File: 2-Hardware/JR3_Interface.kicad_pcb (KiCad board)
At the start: 2 copper layers, 25.4 x 74.2 mm, 11 parts, among them J1 DB9, J2 CONN_3, J3 CONN_3, P1 HE10-34

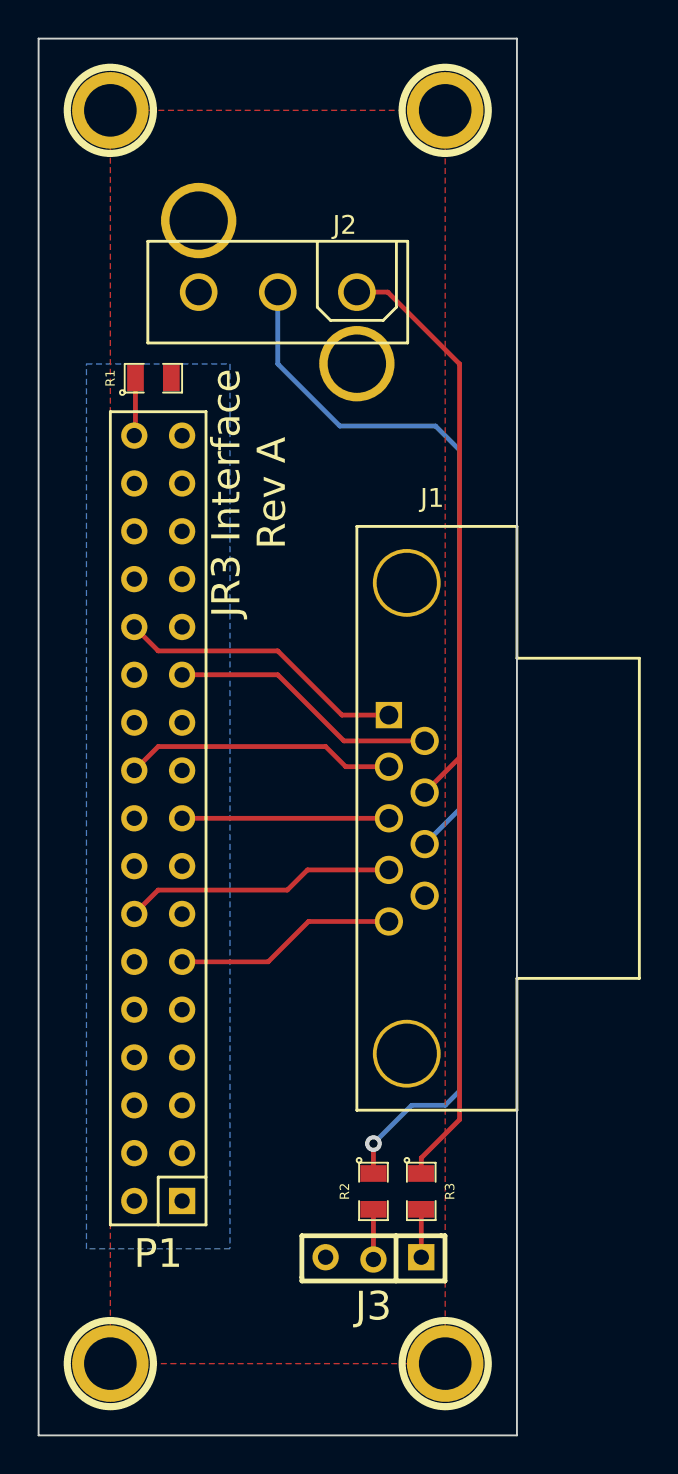
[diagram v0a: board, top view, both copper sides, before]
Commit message: Fixes #5 and resolves #3. Also fixes the power connector footprint on this board.
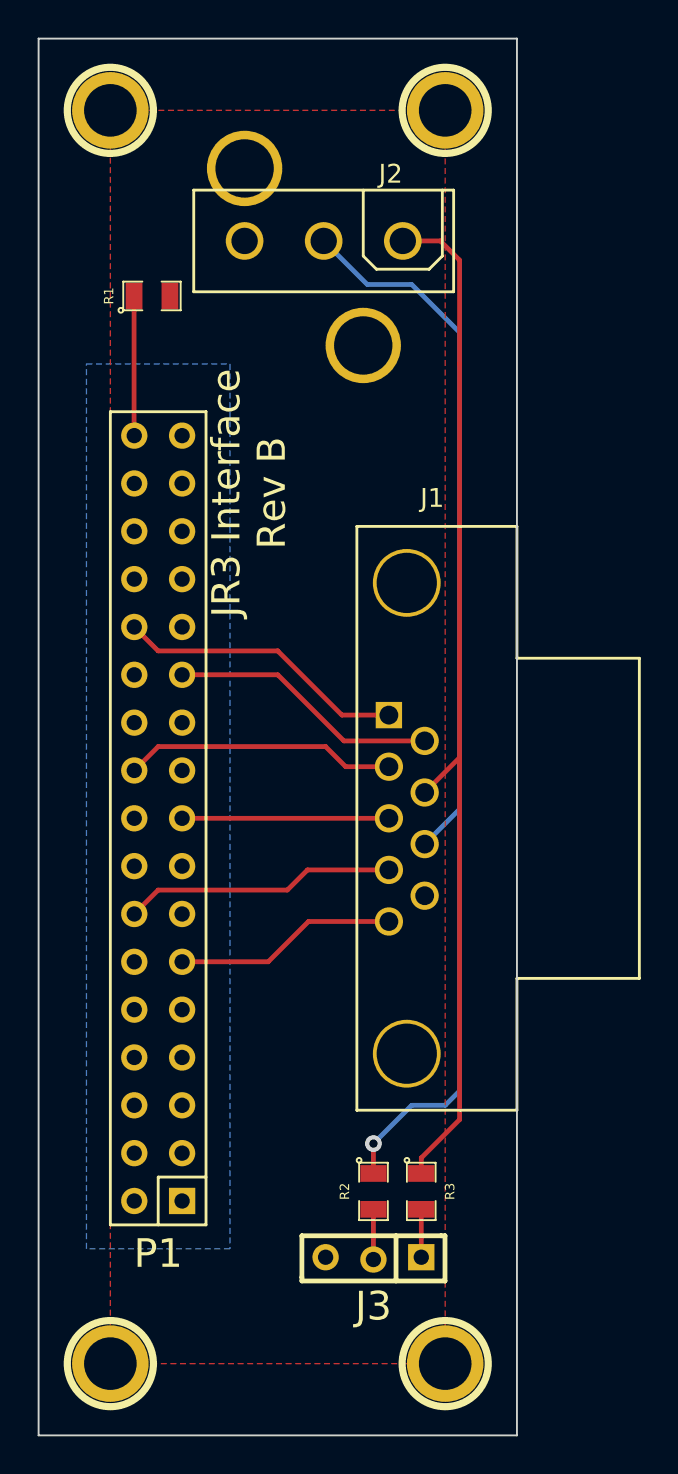
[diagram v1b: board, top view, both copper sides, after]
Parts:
- R1: value R -> 20k
- R2, R3: value R -> 500
- moved R1 4.37 mm to (74.1, 56.8)
- moved J2 3.65 mm to (83.2, 53.9)
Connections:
- P1 pad 12: (no net) -> GND
- P1 pad 15: (no net) -> GND
- P1 pad 18: (no net) -> GND
- P1 pad 21: (no net) -> GND
- P1 pad 24: (no net) -> GND
- P1 pad 27: (no net) -> GND
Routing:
- net /AI_GND: track 3.07 -> 7.48 mm
- net +12V: track 53.7 -> 55.6 mm
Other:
- board text added: "JR3 Interface Rev B"
- board text removed: "JR3 Interface Rev A"
